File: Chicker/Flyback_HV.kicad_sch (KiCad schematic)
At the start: 63 parts, among them Q2 IRFR3410TRPBF, Q3 FGH50T65SQD-F155, Q5 TN2130K1-G, Q6 IPD60R3K4CEAUMA1, Q7 FGH50T65SQD-F155, T1 DA2034, U2 LT3750, U4 MCP14A0454-E/SN

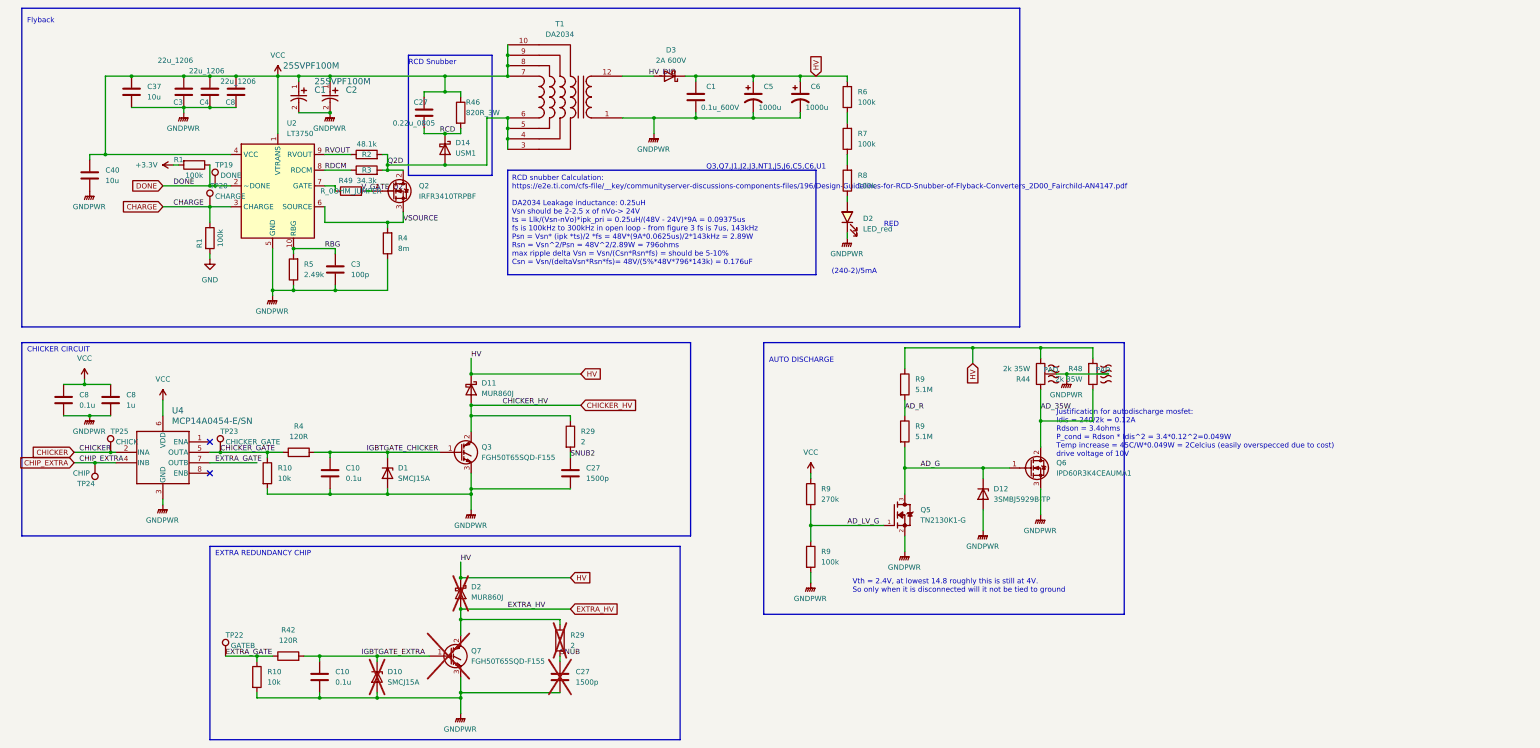
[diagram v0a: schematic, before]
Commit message: update to schematic but something on layout is broken
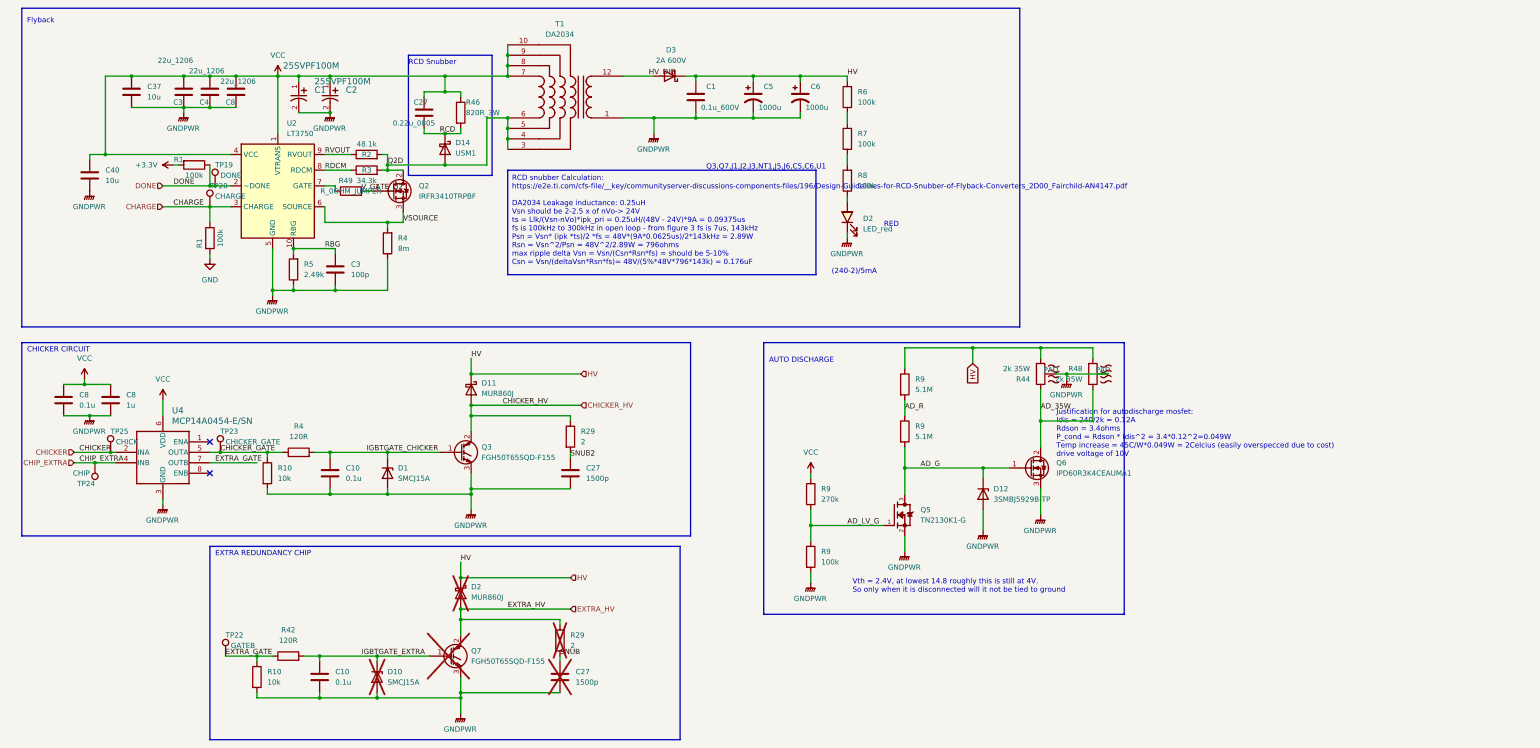
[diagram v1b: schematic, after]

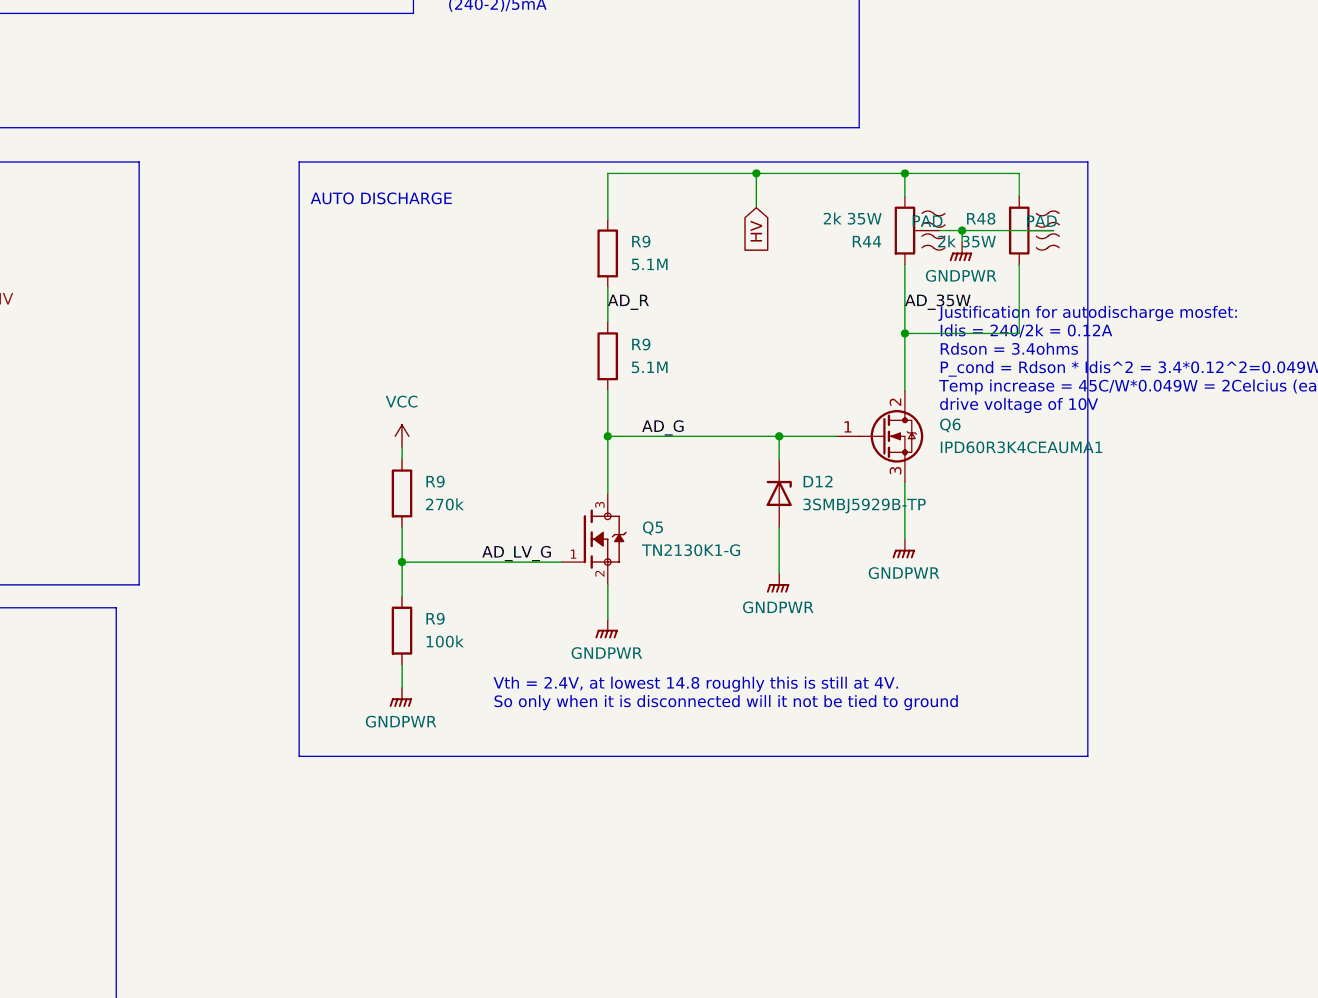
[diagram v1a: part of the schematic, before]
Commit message: midplate 4 layers, chicker shell off limit switch idea
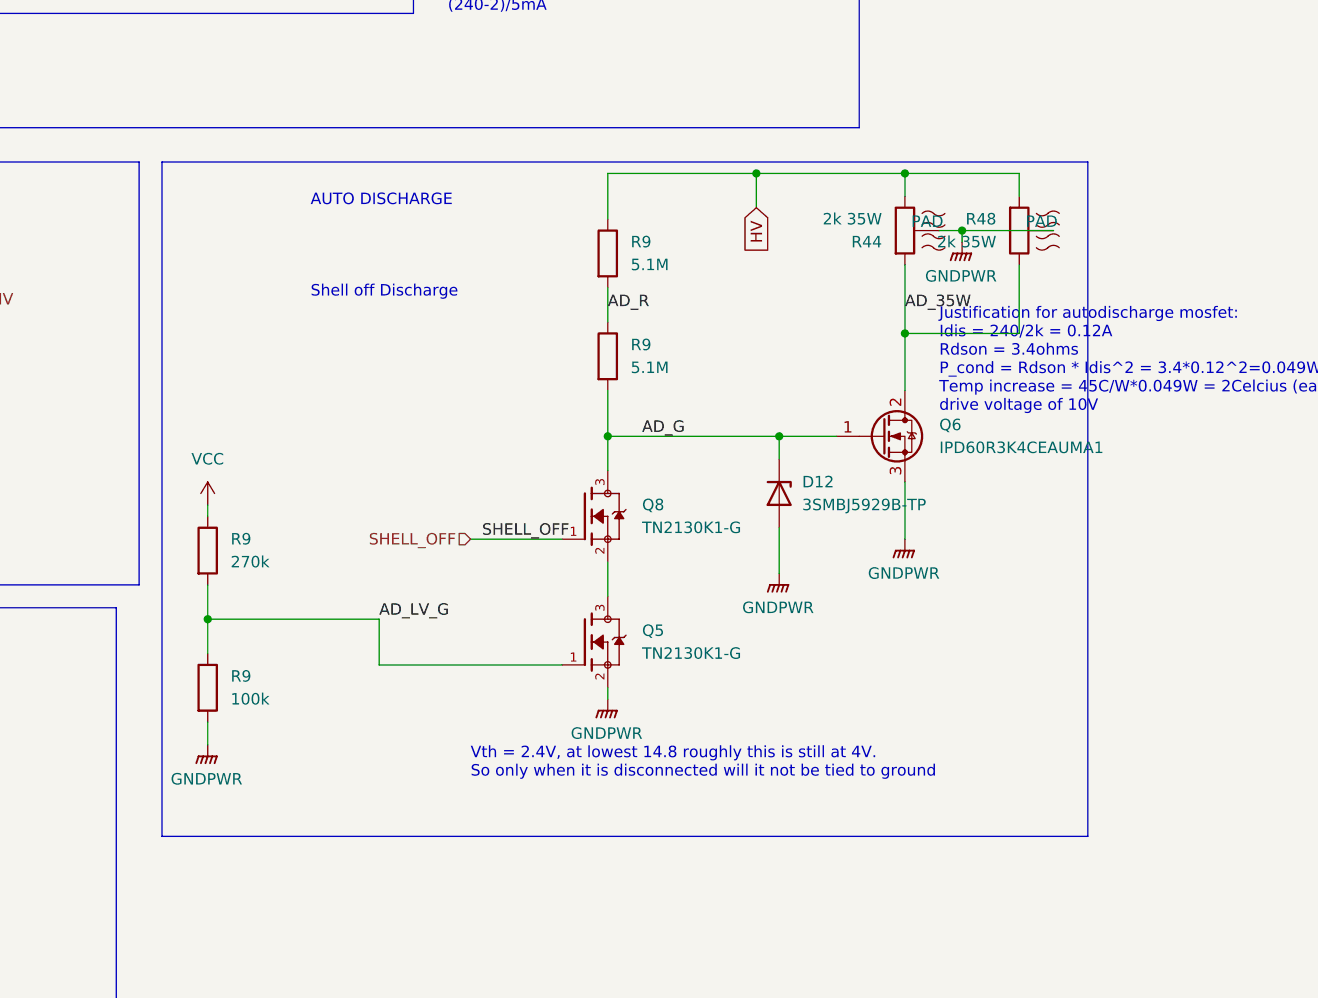
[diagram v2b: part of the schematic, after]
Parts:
- added Q8: TN2130K1-G, bots:SOT95P240X111-3N, symbol bots:TN2130K1-G
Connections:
- net AD_G: now also Q8.3; no longer Q5.3
- new net: Q5.3, Q8.2
- new net SHELL_OFF: Q8.1
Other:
- note added: "Shell off Discharge"
- moved on the sheet: Q5, R9

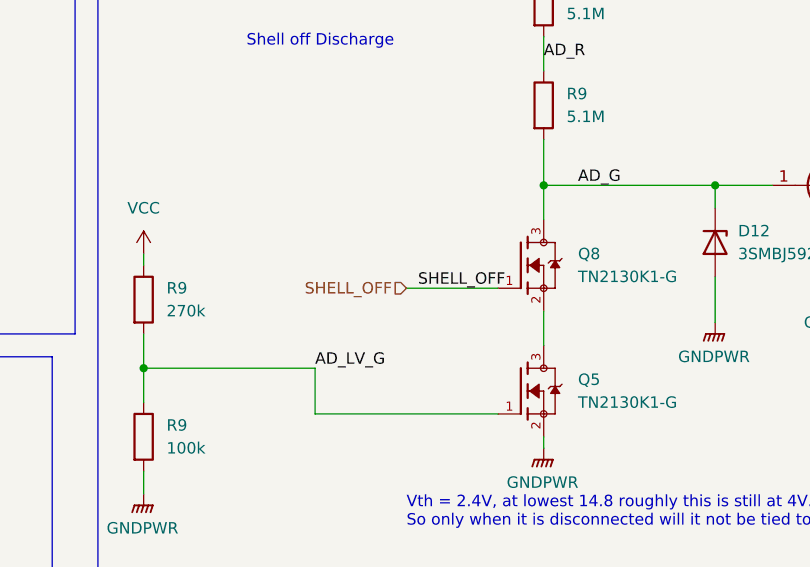
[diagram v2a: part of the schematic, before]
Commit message: chicker discharge HV shell off fixed
pull up to 3v3 and limit switch, input to RP2040, output to inverted discharge signal which discharges if it is set to 0
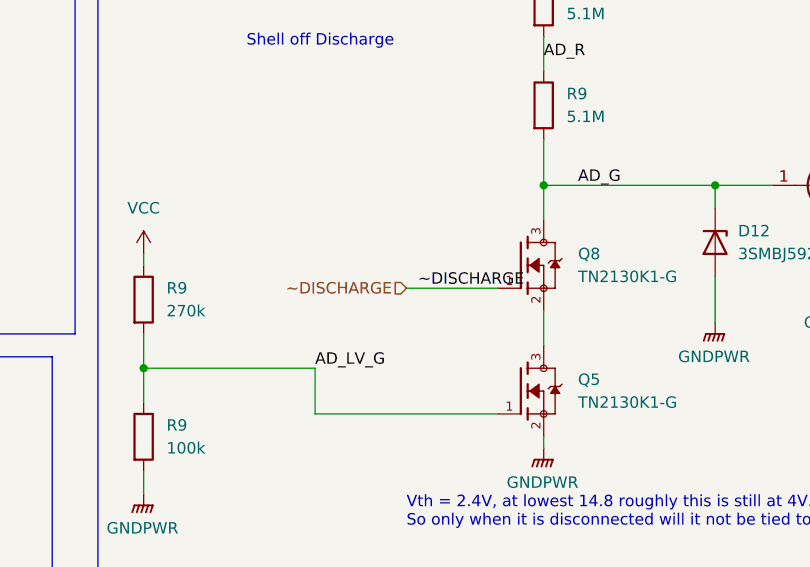
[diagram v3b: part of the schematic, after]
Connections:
- net SHELL_OFF renamed ~DISCHARGE
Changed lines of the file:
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@@
     (effects (font (size 1.27 1.27)) (justify left bottom))
   )
-  (label "SHELL_OFF" (at 215.9 138.43 0) (fields_autoplaced)
+  (label "~DISCHARGE" (at 215.9 138.43 0) (fields_autoplaced)
     (effects (font (size 1.27 1.27)) (justify left bottom))
   )
@@
     (effects (font (size 1.27 1.27)) (justify right))
   )
+  (hierarchical_label "~DISCHARGE" (shape input) (at 214.63 138.43 180) (fields_autoplaced)
+    (effects (font (size 1.27 1.27)) (justify right))
+  )
   (hierarchical_label "DONE" (shape input) (at 49.53 58.42 180) (fields_autoplaced)
     (effects (font (size 1.27 1.27)) (justify right))
@@
     (effects (font (size 1.27 1.27)) (justify left))
   )
-  (hierarchical_label "SHELL_OFF" (shape input) (at 214.63 138.43 180) (fields_autoplaced)
-    (effects (font (size 1.27 1.27)) (justify right))
-  )
   (symbol (lib_id "bots:C_100p") (at 91.44 78.74 0) (unit 1)

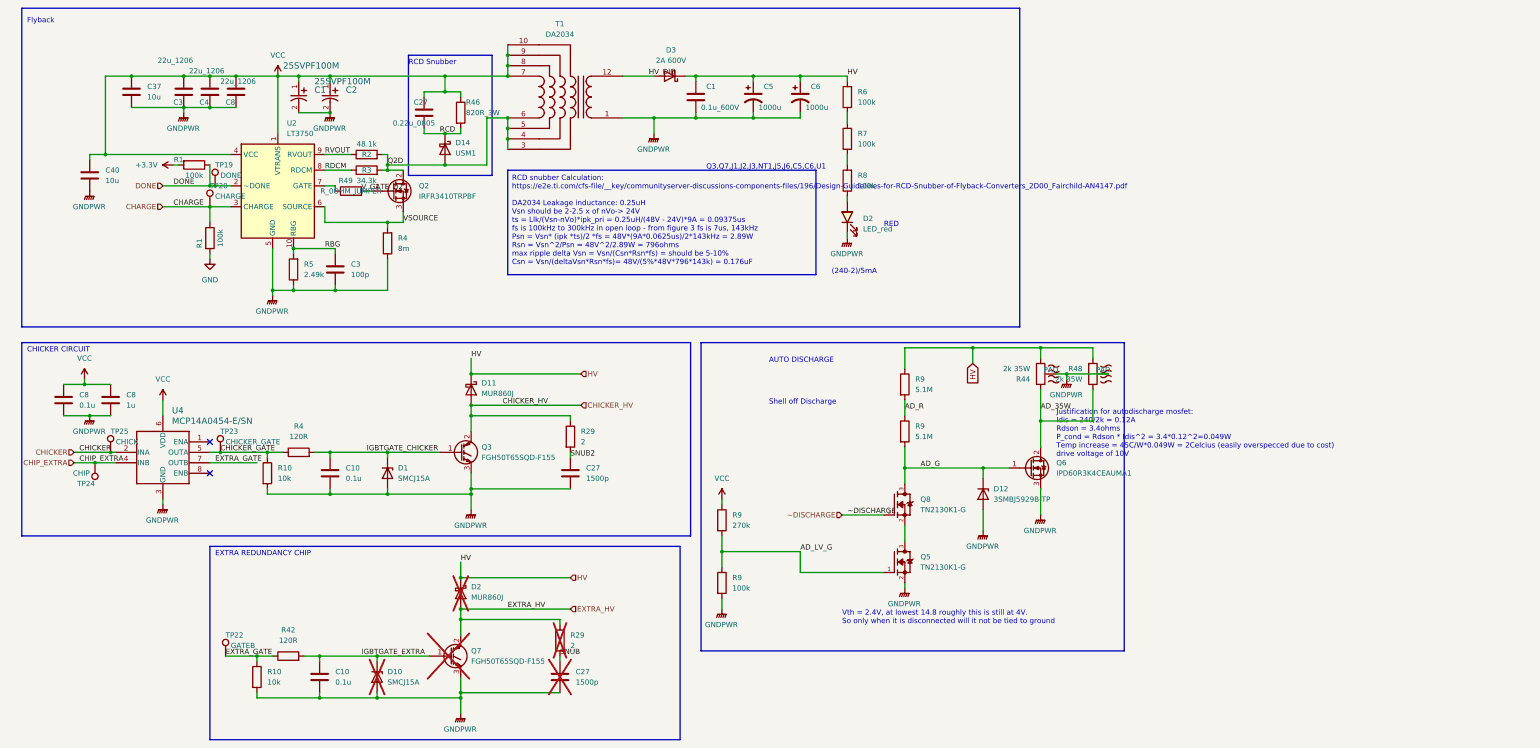
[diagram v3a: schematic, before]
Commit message: chicker discharge circuit finalized
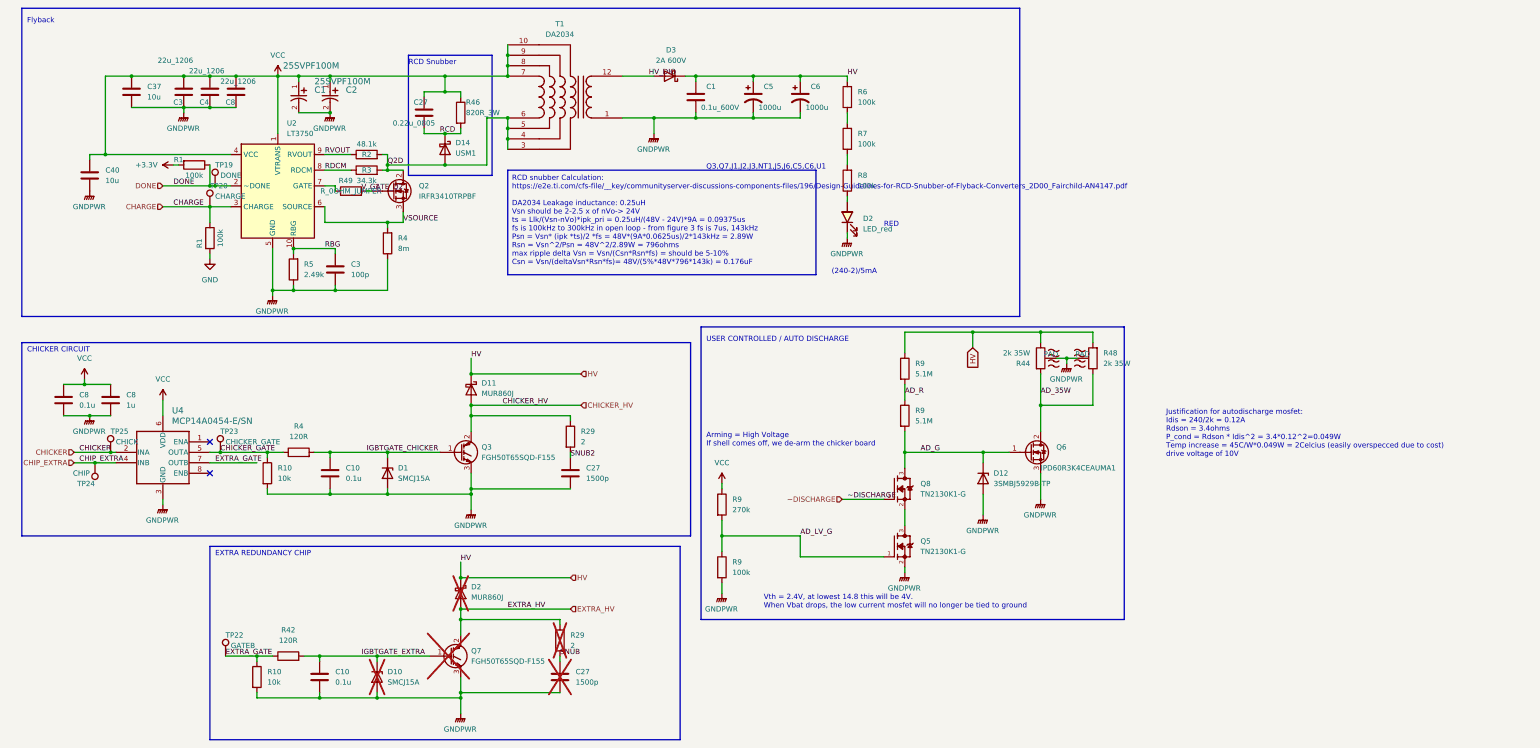
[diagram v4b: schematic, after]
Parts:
- Q8: Price 0.65 -> 0.67
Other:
- note added: "Arming = High Voltage If shell comes off, we de-arm the chicker board"
- note added: "USER CONTROLLED / AUTO DISCHARGE"
- note added: "Vth = 2.4V, at lowest 14.8 this will be 4V. When Vbat drops, the low current mosfet will no longer be tied to ground"
- note removed: "AUTO DISCHARGE"
- note removed: "Shell off Discharge"
- note removed: "Vth = 2.4V, at lowest 14.8 roughly this is still at 4V. So only when it is disconnected will it not be tied to ground"
- moved on the sheet: D12, Q5, Q6, Q8, R44, R48, R9

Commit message: chicker v1.1 changes
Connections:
- net AD_G: now also Q5.3; no longer Q8.3
- net GNDPWR: now also Q8.2; no longer Q5.2
- new net: Q5.2, Q8.3
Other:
- moved on the sheet: R9
